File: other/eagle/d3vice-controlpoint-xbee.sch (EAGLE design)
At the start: 15 parts, among them IC3 74LS125N

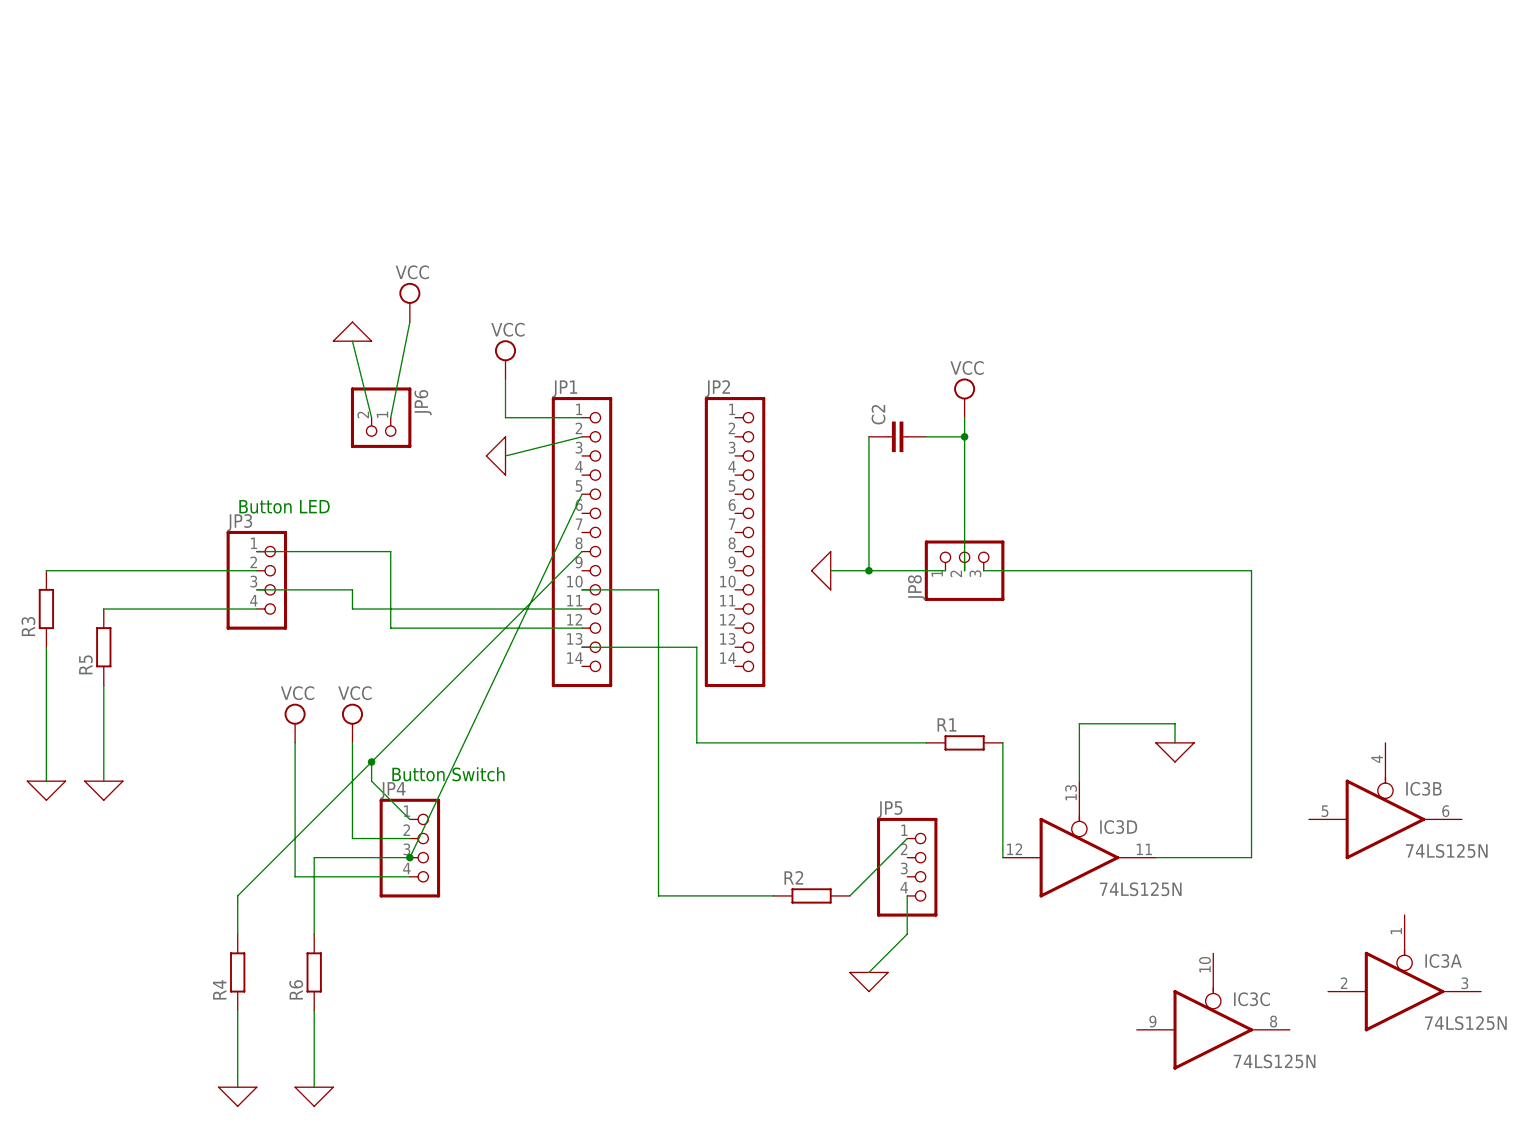
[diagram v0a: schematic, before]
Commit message: added battery voltage circuit
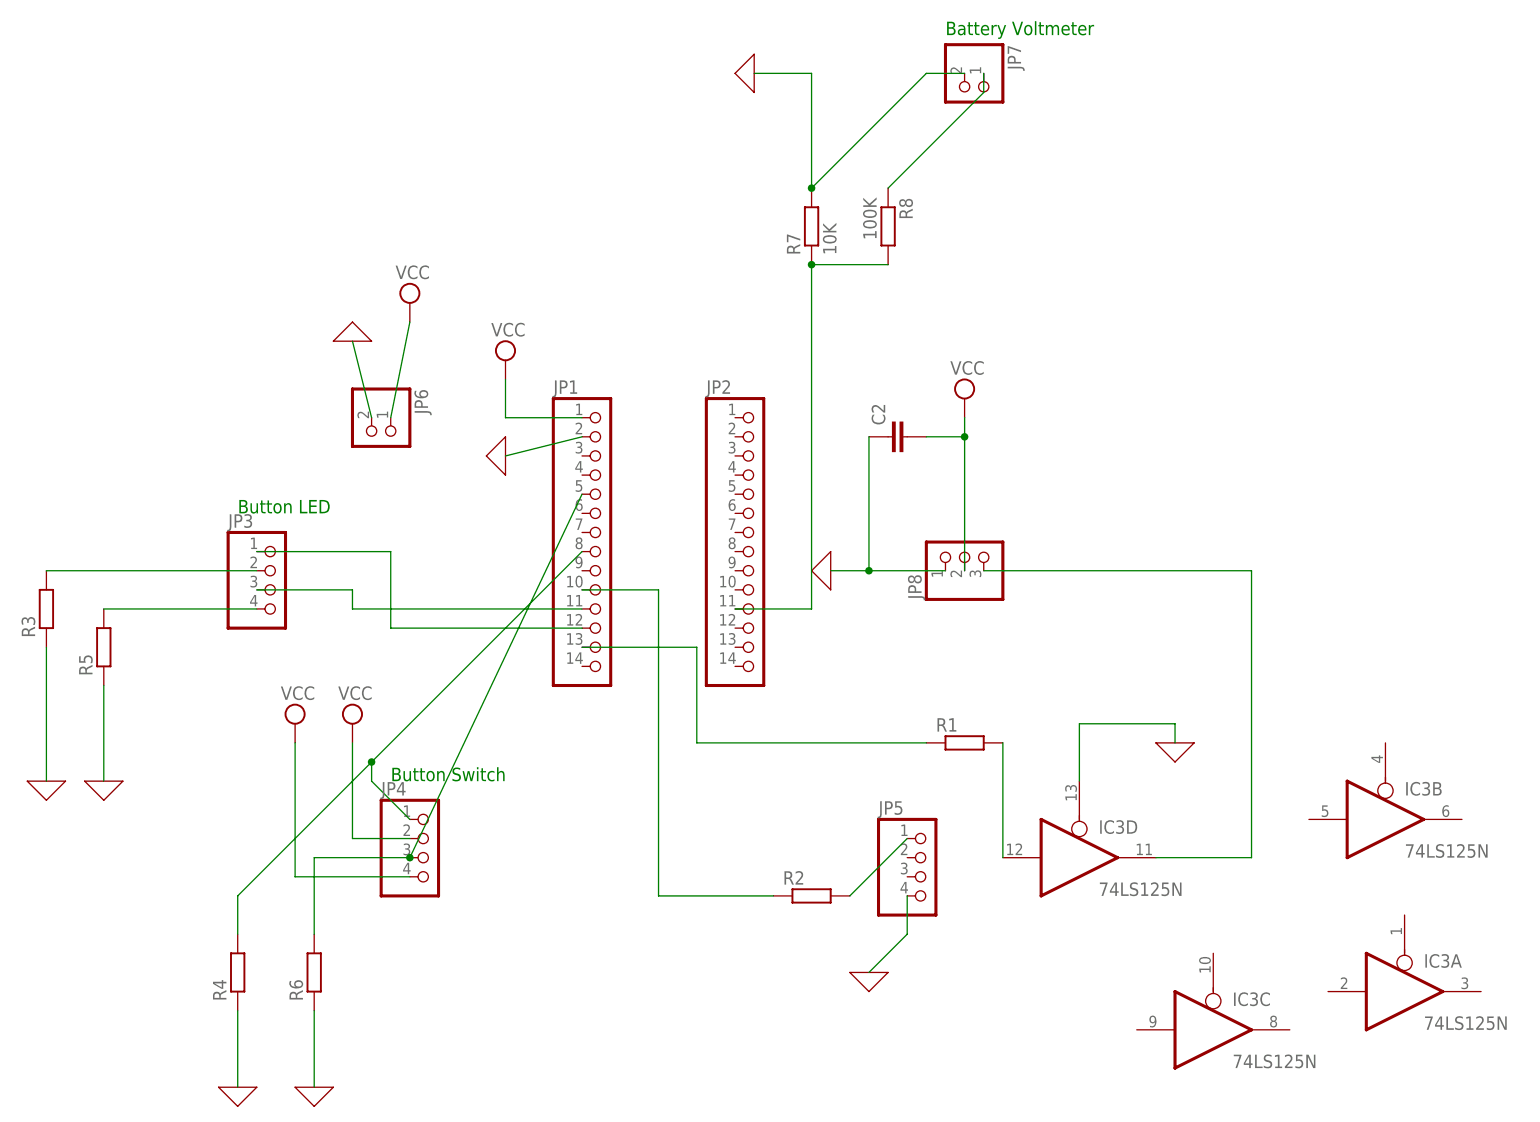
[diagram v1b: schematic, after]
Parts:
- added JP7: (no value), pinhead:PINHD-1X2
- added R7: 10K, eagle-ltspice:R0204/7
- added R8: 100K, eagle-ltspice:R0204/7
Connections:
- new net 0: JP7.2, R7.2
- new net N$1: JP2.11, R7.1, R8.2
- new net N$12: JP7.1, R8.1
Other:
- note added: "Battery Voltmeter"
